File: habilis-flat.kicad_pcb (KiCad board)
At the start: 2 copper layers, 164.5 x 172.8 mm, 74 parts, among them J1 AudioJack4, SW1 MX, SW10 MX, SW11 MX, SW12 MX, SW13 MX, SW14 MX, SW15 MX, SW16 MX, SW17 MX, SW18 MX, SW19 MX, SW2 MX, SW20 MX, SW21 MX, SW22 MX, SW23 MX, SW24 MX, SW25 MX, SW26 MX, SW27 MX, SW28 MX, SW29 MX, SW3 MX, SW30 MX, SW31 MX, SW32 MX, SW33 MX, SW34 MX, SW35 MX, SW4 MX, SW5 MX, SW6 MX, SW7 MX, SW8 MX, SW9 MX, U1 ProMicro

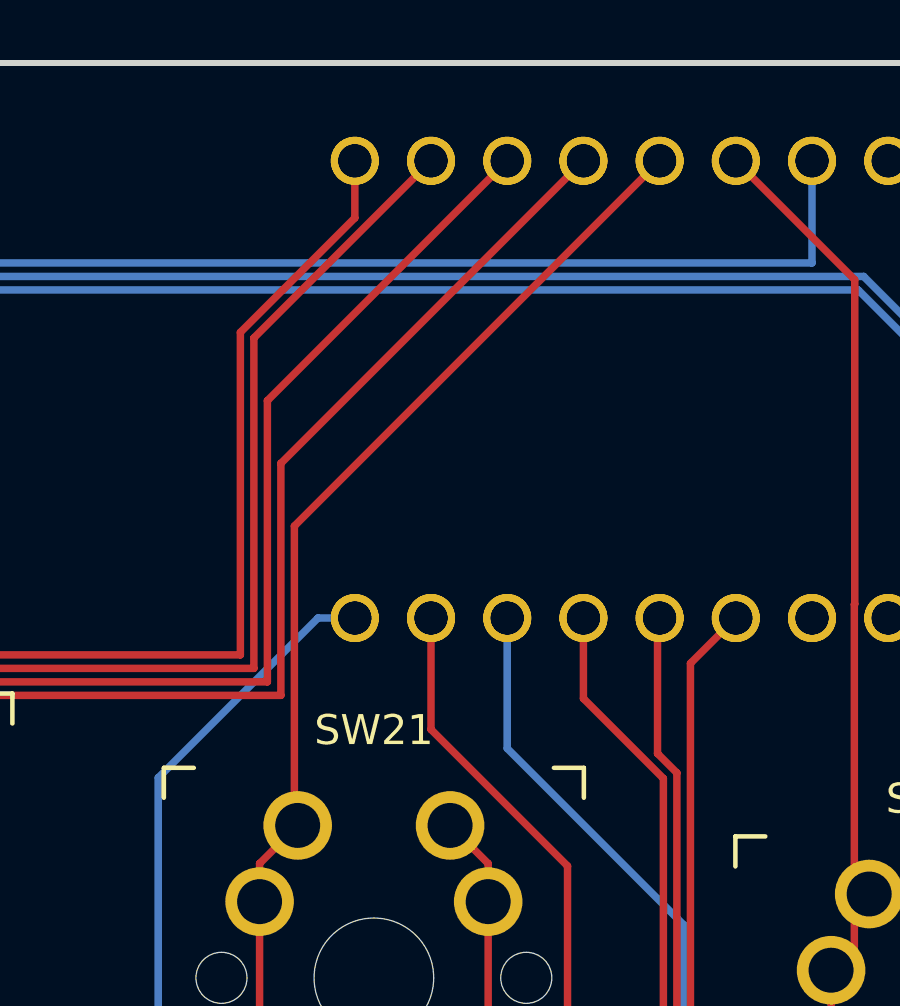
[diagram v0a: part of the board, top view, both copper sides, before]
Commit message: Add silkscreen signature
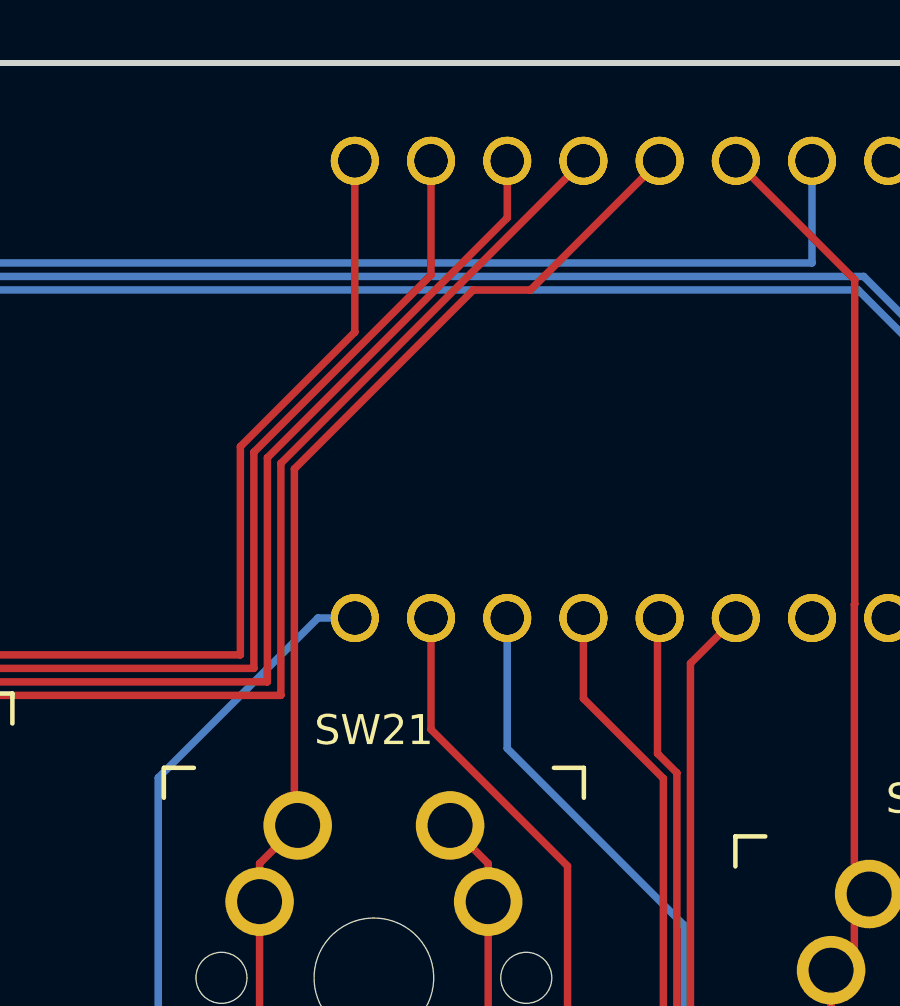
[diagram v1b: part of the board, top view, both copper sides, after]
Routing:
- net Net-(U1-C6): track 118.8 -> 119.9 mm
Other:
- board text added: "Copyright © 2023 Thibault Polge https://thb.lt/"
- board text added: "FLAT"
- board text added: "HABILIS"
- board text added: "LAYOUT TEST PROTOTYPE REV 0"

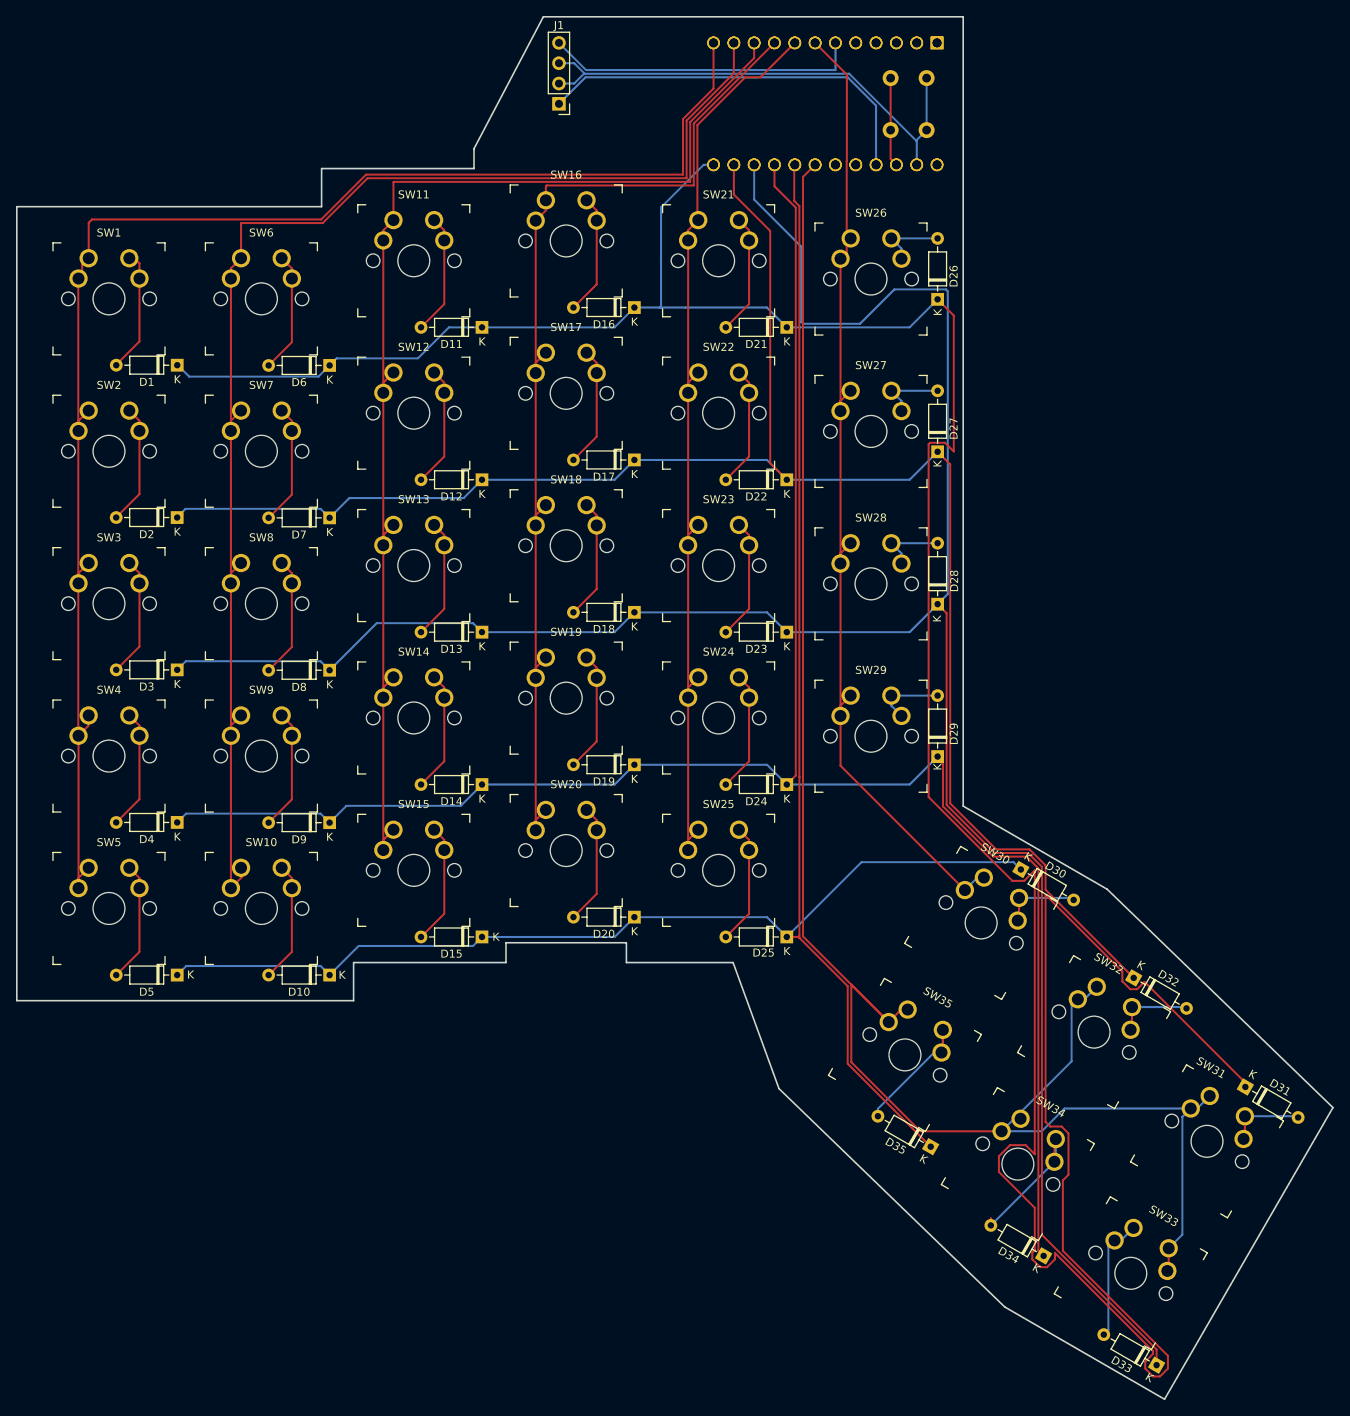
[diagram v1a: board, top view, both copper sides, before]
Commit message: Make profile shape even sharper
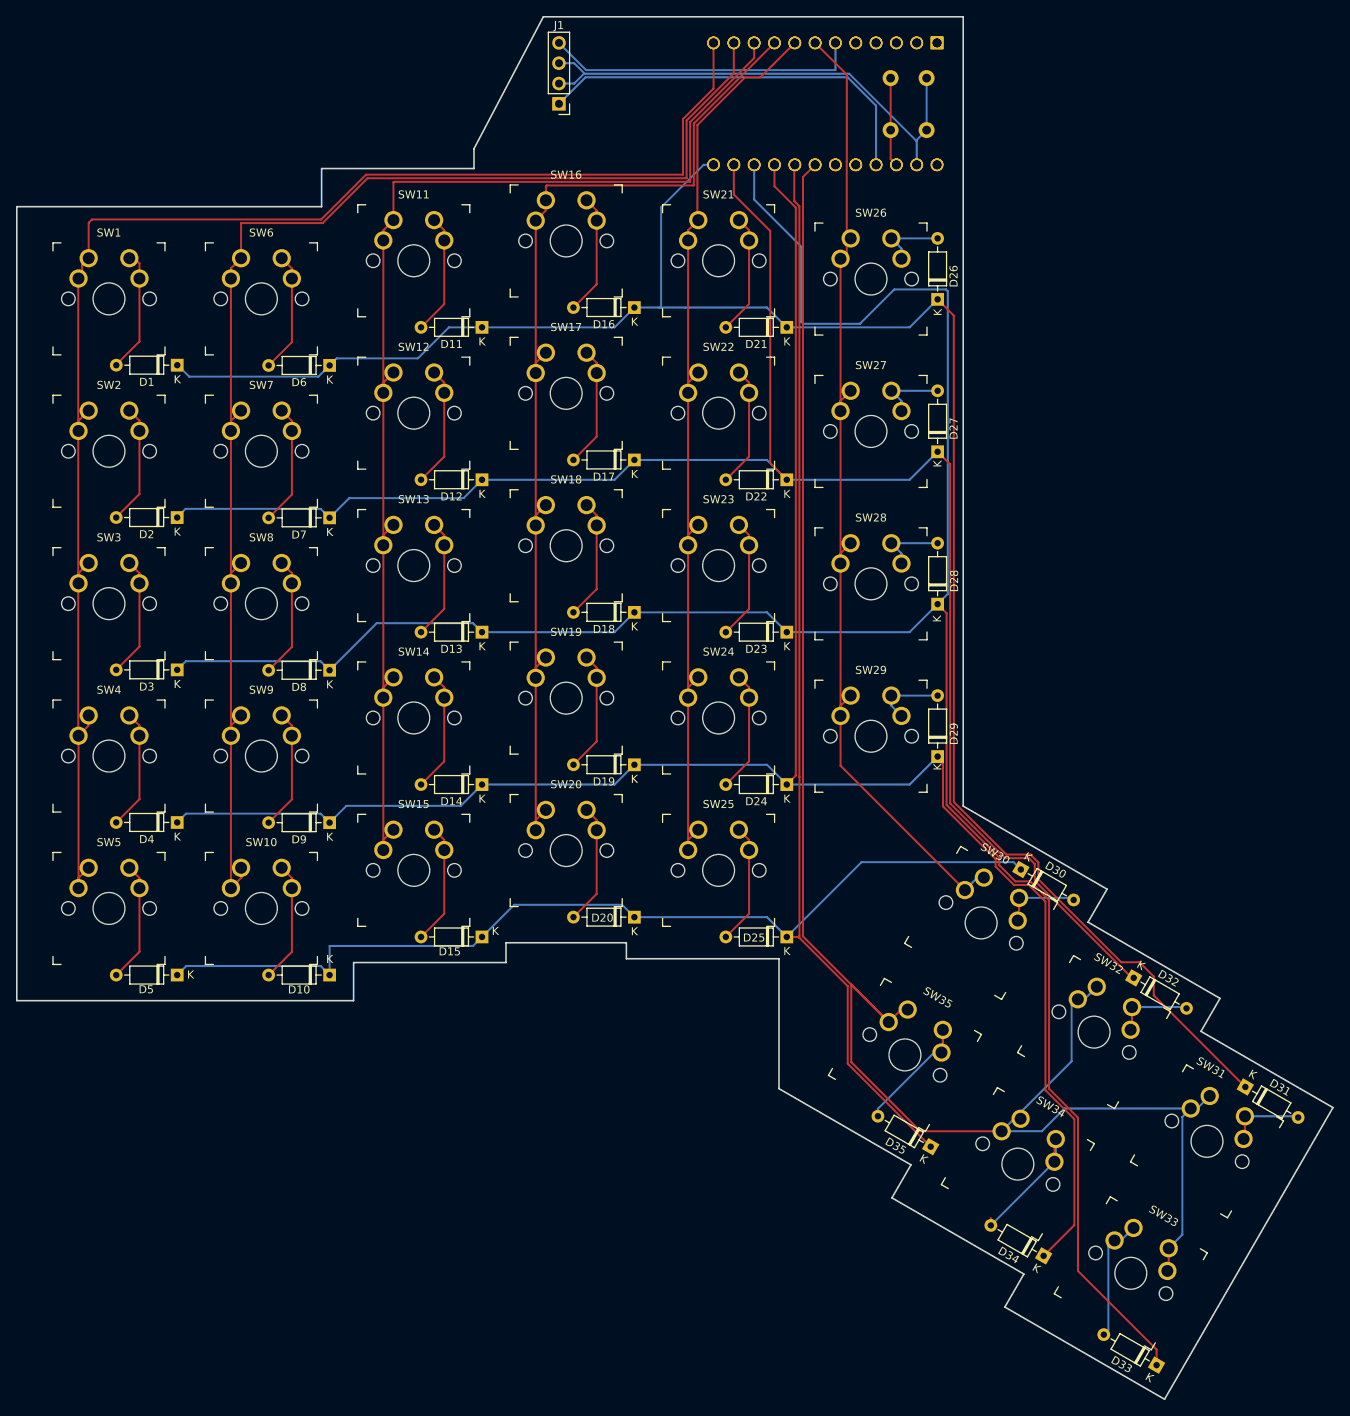
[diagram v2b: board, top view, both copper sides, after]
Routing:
- net Net-(D1-K): track 396.7 -> 240.8 mm
- net Net-(D10-K): track 246.1 -> 249.6 mm
- net Net-(D14-K): track 250.8 -> 252.7 mm
- net Net-(D13-K): track 293.3 -> 291.9 mm
- net Net-(D12-K): track 221.9 -> 221.3 mm
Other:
- outline, holes or cut-outs redrawn
